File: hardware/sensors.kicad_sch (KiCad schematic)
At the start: 1 part, among them U3 BME280

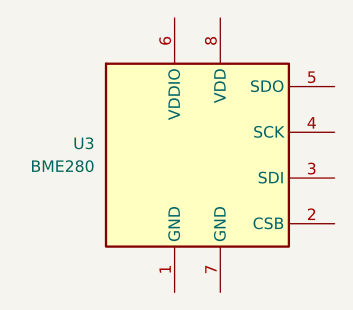
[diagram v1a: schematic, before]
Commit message: update usb port, esd, lcsc
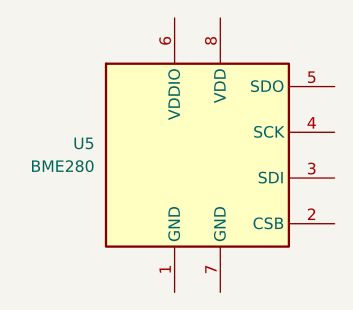
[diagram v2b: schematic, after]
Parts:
- renumbered U3 to U5
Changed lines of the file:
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@@
 		(dnp no)
 		(fields_autoplaced yes)
-		(property "Reference" "U3"
+		(property "Reference" "U5"
 			(at 69.85 60.9599 0)
 			(effects
@@
 			(project "badge"
 				(path "/dc4a3d77-b0f8-4e90-a4be-3e93c7025348/f56a97b8-cdf4-4860-a0f6-235c1ed6139a"
-					(reference "U3")
+					(reference "U5")
 					(unit 1)
 				)

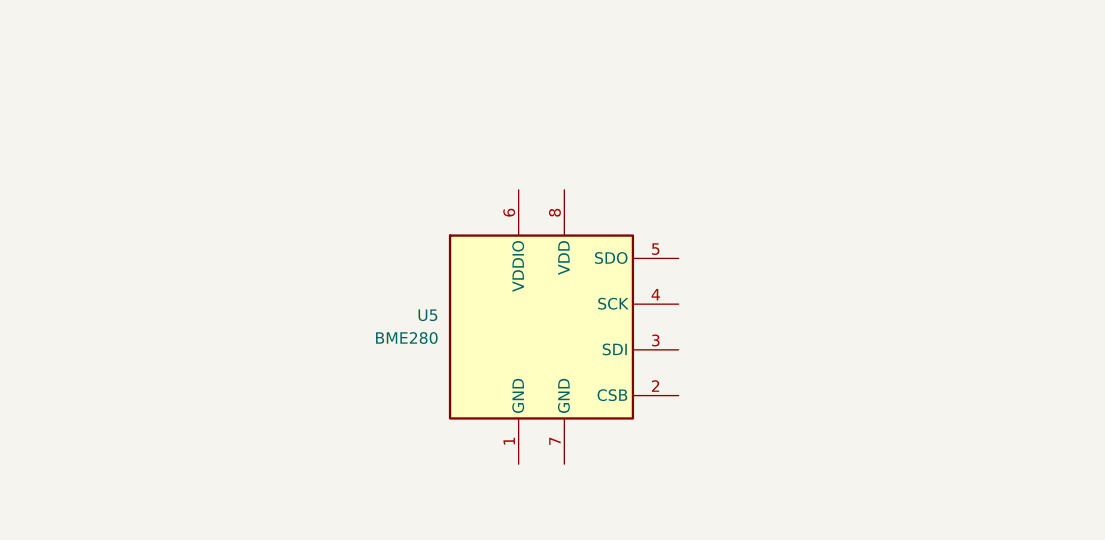
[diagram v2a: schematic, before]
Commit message: add bme280
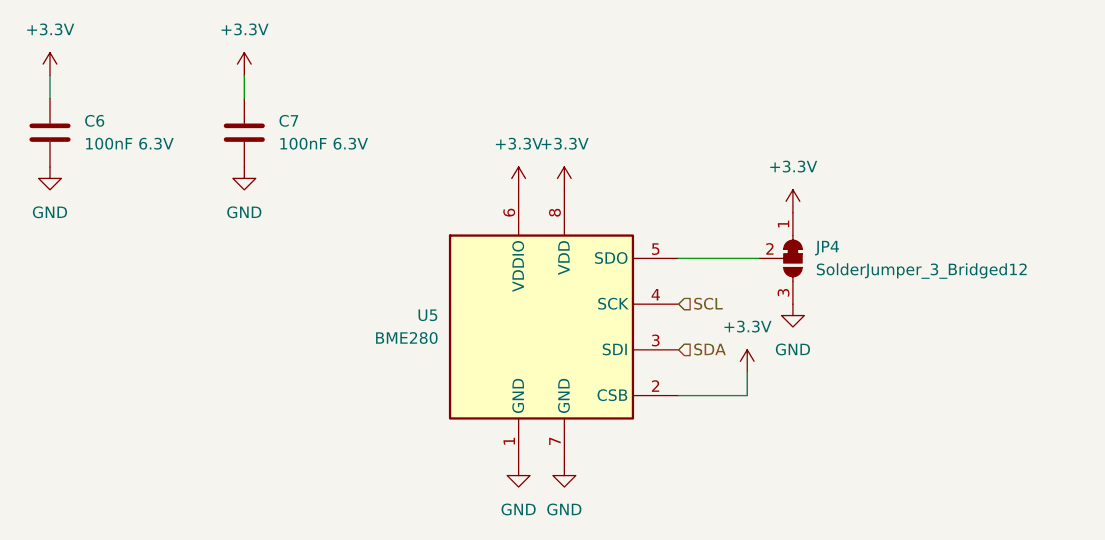
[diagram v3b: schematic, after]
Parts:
- added C6, C7: 100nF 6.3V, Capacitor_SMD:C_0402_1005Metric, symbol Device:C
- added JP4: SolderJumper_3_Bridged12, Jumper:SolderJumper-3_P1.3mm_Bridged12_RoundedPad1.0x1.5mm, symbol Jumper:SolderJumper_3_Bridged12
- U5: LCSC (none) -> C92489
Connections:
- net GND: now reaches U5.1 (GND)
- net GND: now also U5.7 (GND), C6.2, C7.2, JP4.3 (B)
- net +3.3V: now reaches U5.2 (CSB)
- net +3.3V: now also U5.6 (VDDIO), U5.8 (VDD), C6.1, C7.1, JP4.1 (A)
- net SDA: now reaches U5.3 (SDI)
- net SCL: now reaches U5.4 (SCK)
- net at U5.5 (SDO): now also JP4.2 (C)

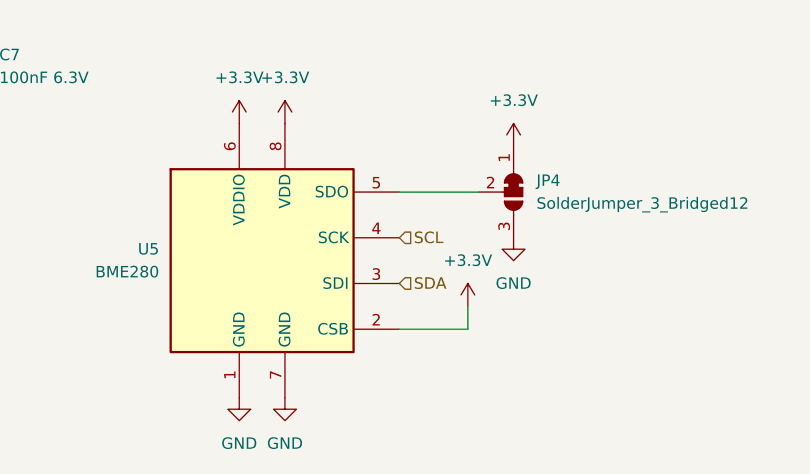
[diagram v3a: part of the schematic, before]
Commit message: lcd wires, wire direction
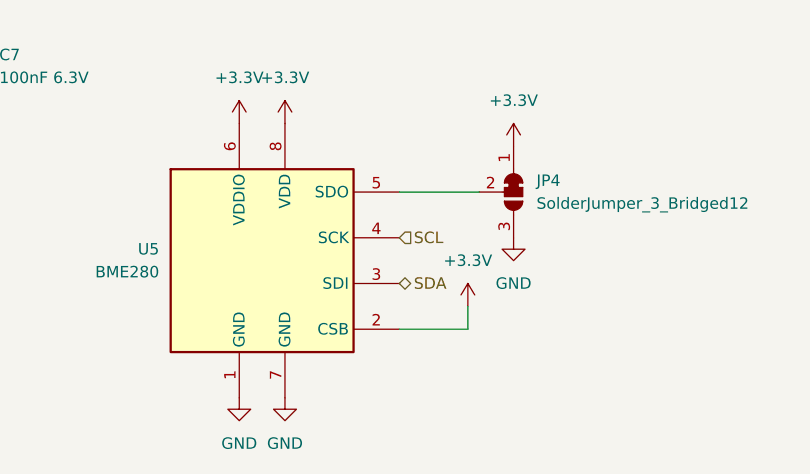
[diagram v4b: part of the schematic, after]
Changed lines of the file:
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@@
 	)
 	(hierarchical_label "SDA"
-		(shape input)
+		(shape bidirectional)
 		(at 96.52 64.77 0)
 		(fields_autoplaced yes)

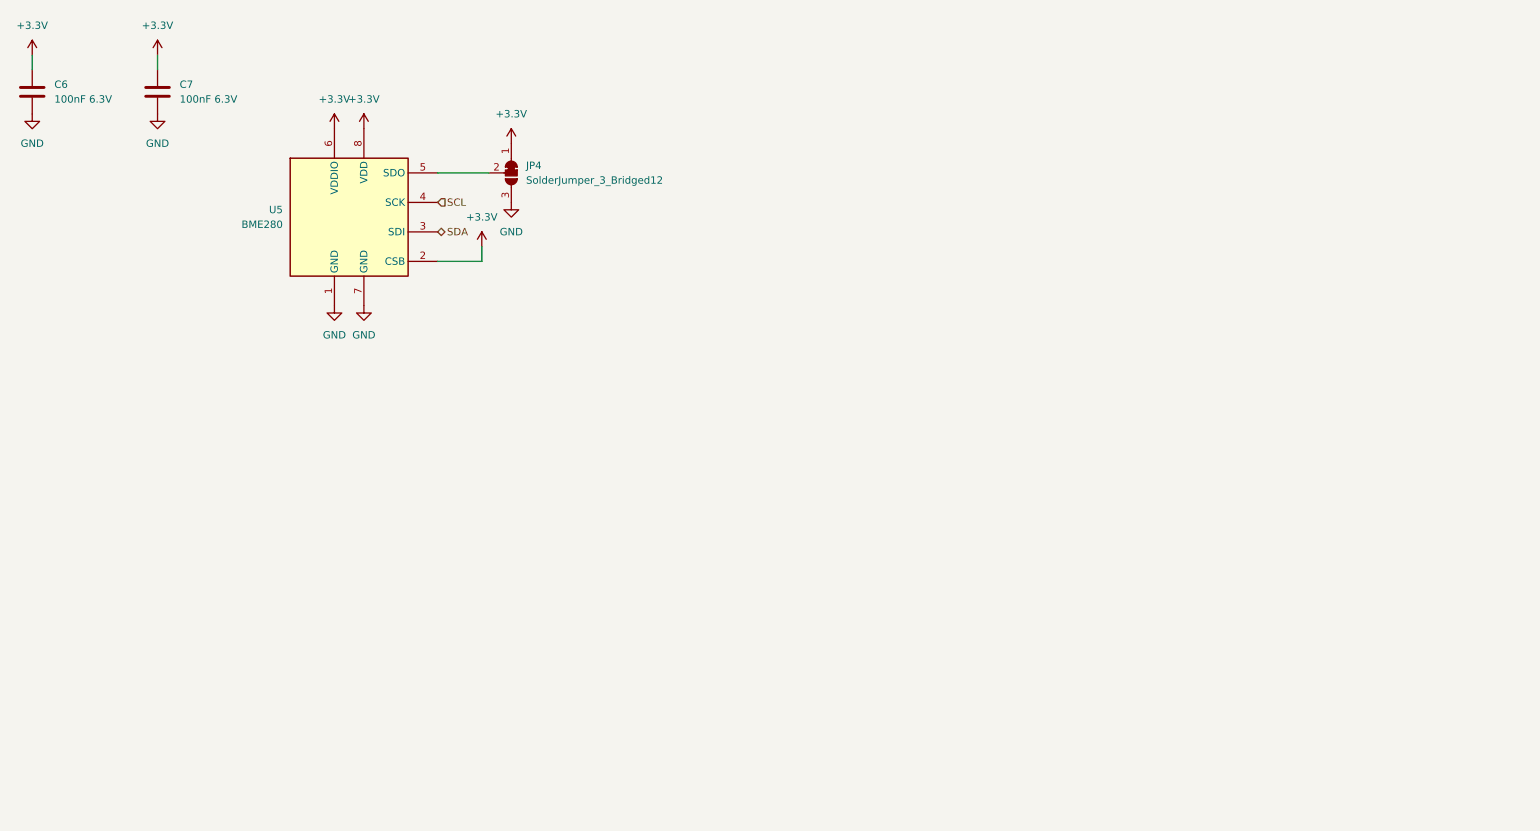
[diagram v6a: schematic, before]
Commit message: Beautified schematic, added I2C addresses
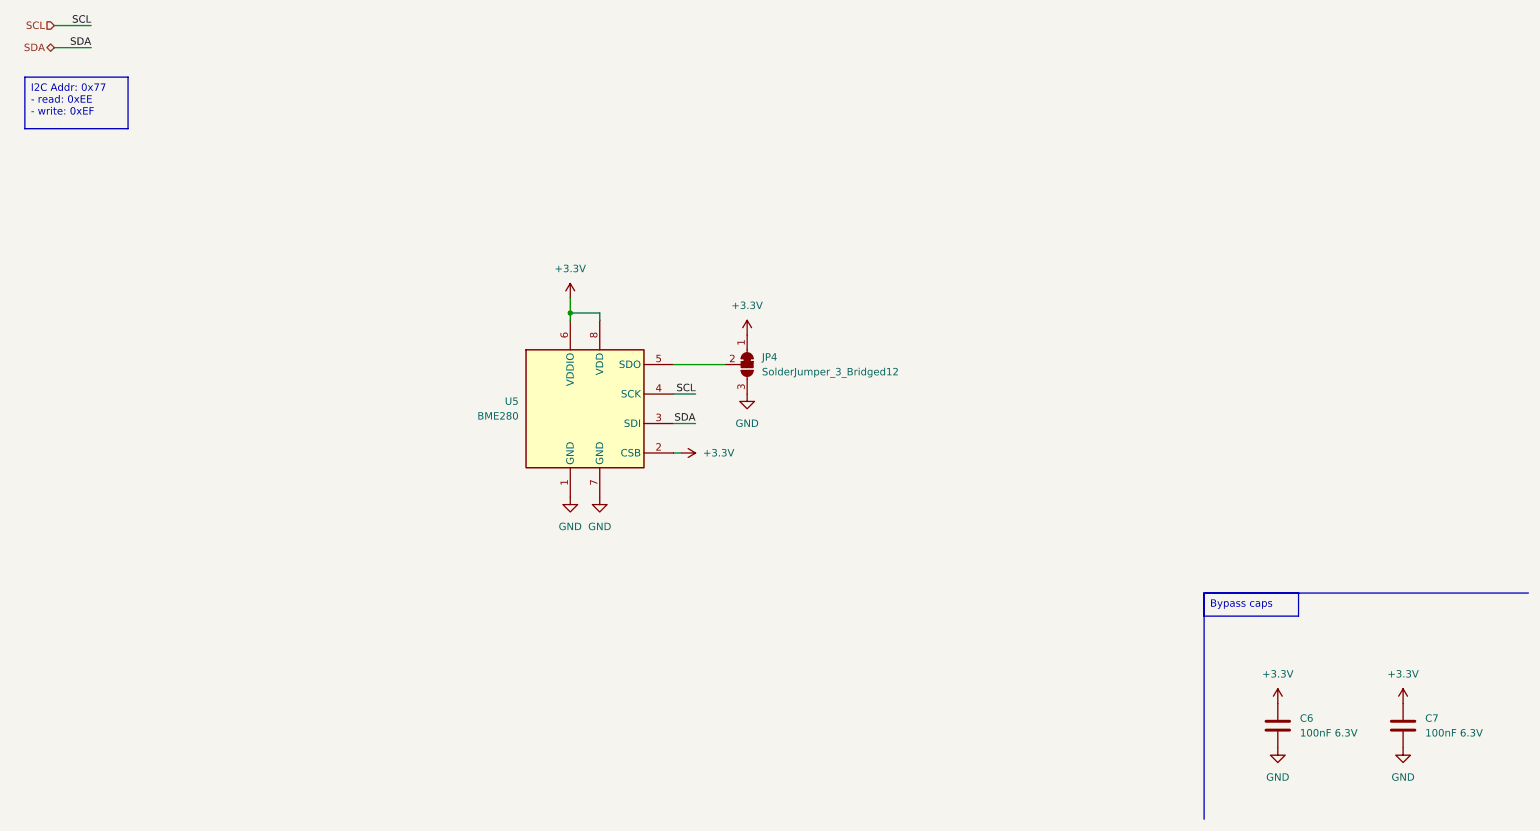
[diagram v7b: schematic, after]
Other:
- moved on the sheet: C6, C7, JP4, U5
